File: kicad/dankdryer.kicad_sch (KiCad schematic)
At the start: 20 parts, among them J13 barreljack, J9 UART, SW2 boot, U1 AP63203WU, U6 ESP32-C6-MINI-1U

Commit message: tighten
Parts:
- L1: value 2.2u -> 3.9u
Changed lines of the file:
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@@
 			)
 		)
-		(property "Value" "2.2u"
+		(property "Value" "3.9u"
 			(at 109.22 39.37 90)
 			(effects

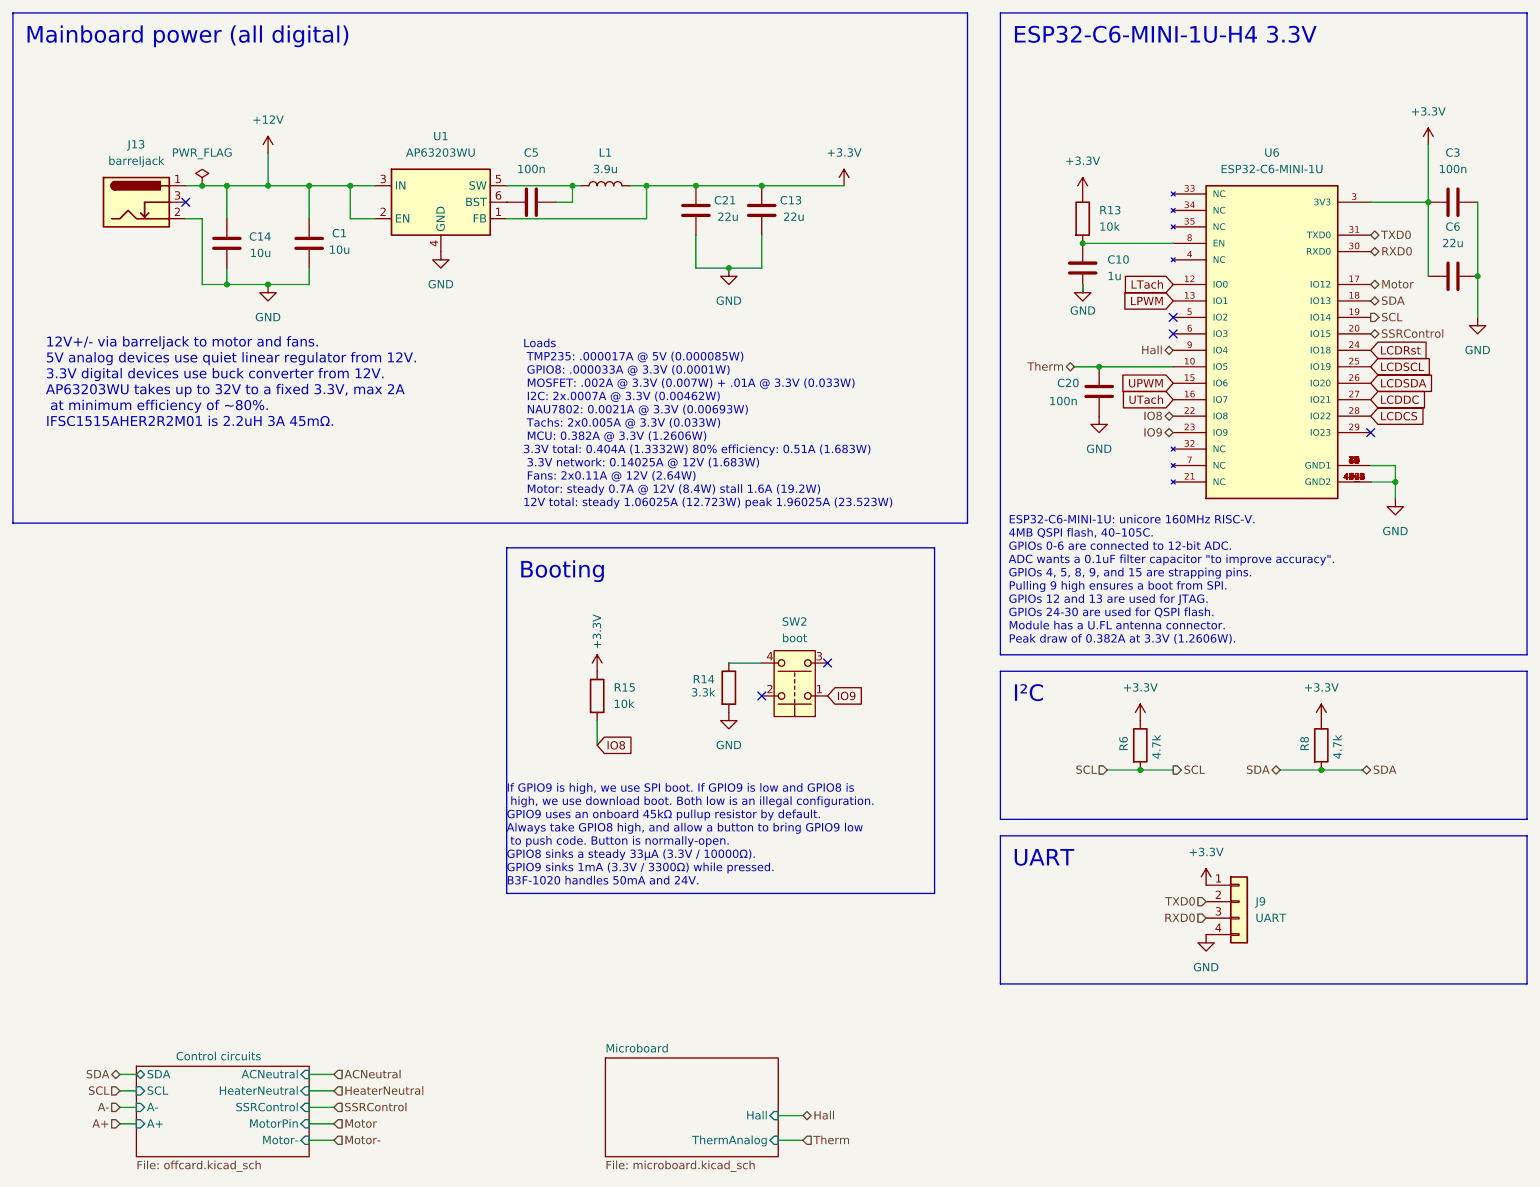
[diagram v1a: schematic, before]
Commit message: back to the tps62132rtgr after all. efficiency!
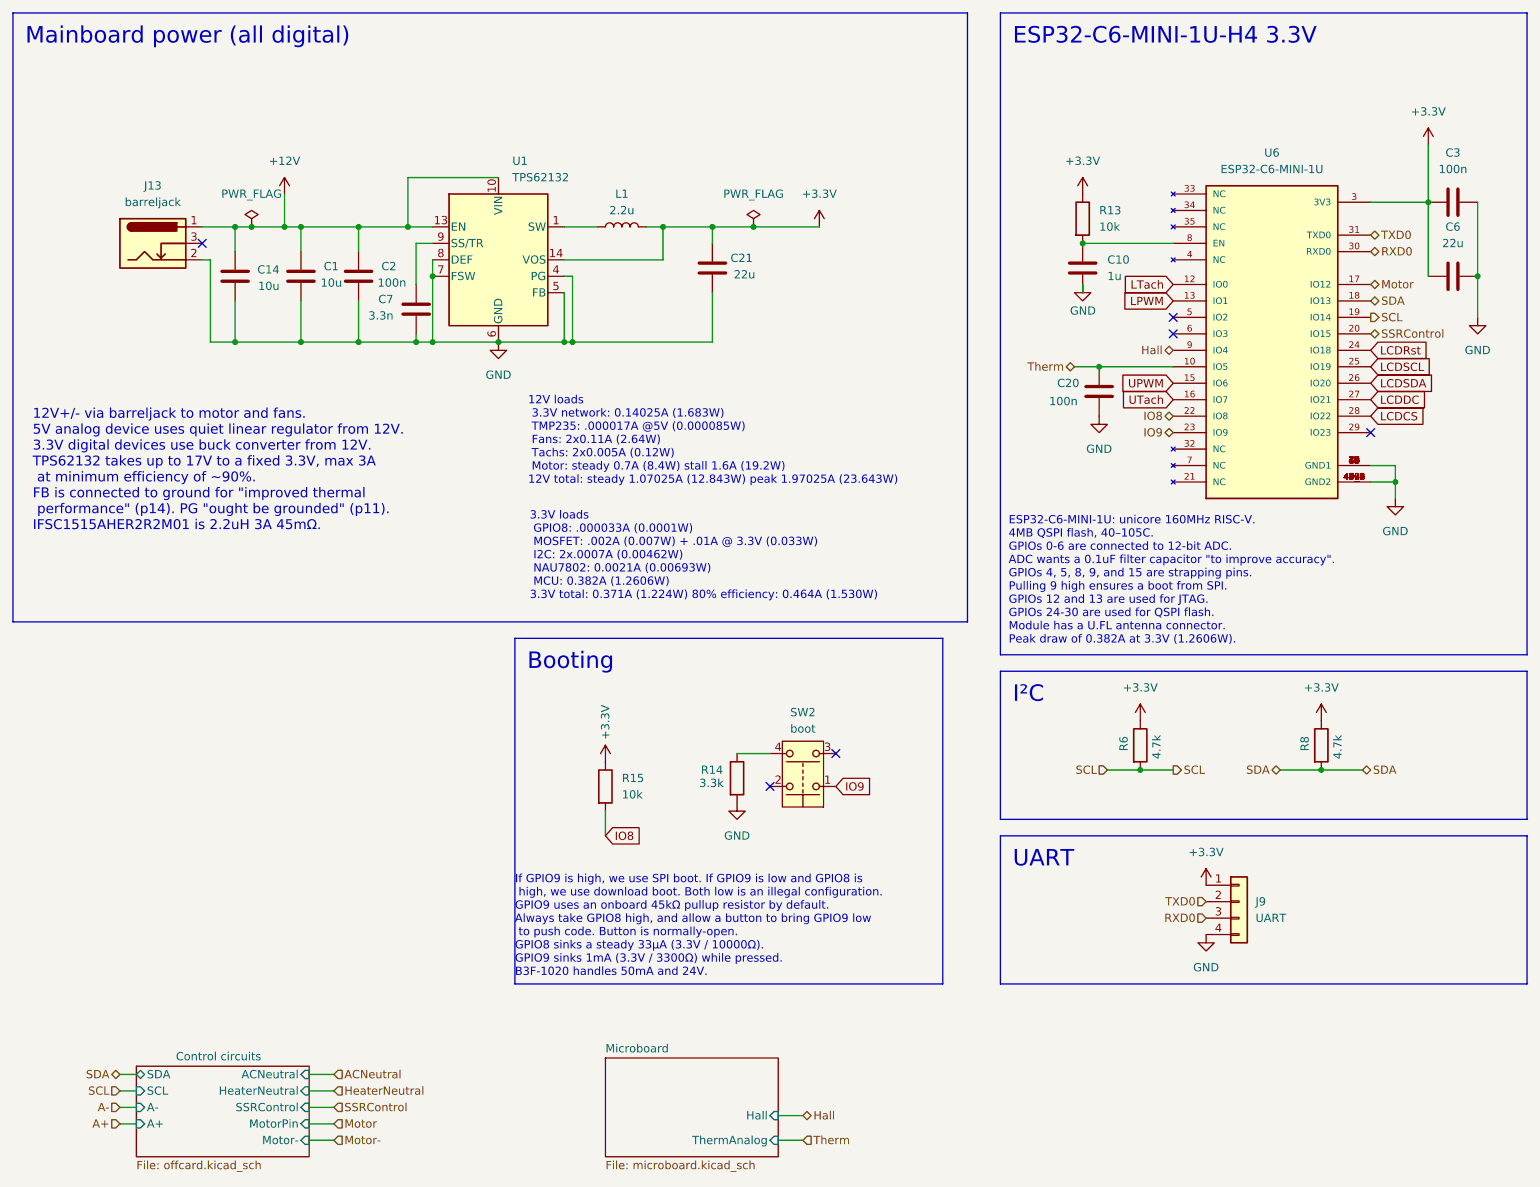
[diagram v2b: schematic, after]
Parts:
- removed C13: 22u, Capacitor_SMD:C_0805_2012Metric_Pad1.18x1.45mm_HandSolder, symbol Device:C
- removed C5: 100n, Capacitor_SMD:C_0805_2012Metric_Pad1.18x1.45mm_HandSolder, symbol Device:C
- removed U1: AP63203WU, Package_TO_SOT_SMD:TSOT-23-6, symbol Regulator_Switching:AP63203WU
- added C2: 100n, Capacitor_SMD:C_0805_2012Metric_Pad1.18x1.45mm_HandSolder, symbol Device:C
- added C7: 3.3n, Capacitor_SMD:C_0805_2012Metric_Pad1.18x1.45mm_HandSolder, symbol Device:C
- added U1: TPS62132, Package_DFN_QFN:VQFN-16-1EP_3x3mm_P0.5mm_EP1.68x1.68mm_ThermalVias, symbol Regulator_Switching:TPS62132
- L1: value 3.9u -> 2.2u
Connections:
- net +12V: now also C2.1, U1.10 (VIN), U1.11 (VIN), U1.12 (VIN), U1.13 (EN)
- net +3.3V: now also U1.14 (VOS)
- net GND: now also C2.2, C7.2, U1.15 (GND), U1.16 (GND), U1.17 (GND), U1.4 (PG), U1.5 (FB), U1.6 (GND), U1.7 (FSW), U1.8 (DEF)
- net at L1.1: now also U1.1 (SW), U1.2 (SW), U1.3 (SW)
- new net: C7.1, U1.9 (SS/TR)
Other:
- note added: "12V loads 3.3V network: 0.14025A (1.683W) TMP235: .000017A @5V (0.000085W) Fans: 2x0.11A (2.64W) Tachs: 2x0.005A (0.12W) Motor: steady 0.7A (8.4W) stall 1.6A (19.2W) 12V total: steady 1.07025A (12.843W) peak 1.97025A (23.643W)"
- note added: "12V+/- via barreljack to motor and fans. 5V analog device uses quiet linear regulator from 12V. 3.3V digital devices use buck converter from 12V. TPS62132 takes up to 17V to a fixed 3.3V, max 3A at minimum efficiency of ~90%. FB is connected to ground for "improved thermal performance" (p14). PG "ought be grounded" (p11). IFSC1515AHER2R2M01 is 2.2uH 3A 45mΩ."
- note added: "3.3V loads GPIO8: .000033A (0.0001W) MOSFET: .002A (0.007W) + .01A @ 3.3V (0.033W) I2C: 2x.0007A (0.00462W) NAU7802: 0.0021A (0.00693W) MCU: 0.382A (1.2606W) 3.3V total: 0.371A (1.224W) 80% efficiency: 0.464A (1.530W)"
- note removed: "12V+/- via barreljack to motor and fans. 5V analog devices use quiet linear regulator from 12V. 3.3V digital devices use buck converter from 12V. AP63203WU takes up to 32V to a fixed 3.3V, max 2A at minimum efficiency of ~80%. IFSC1515AHER2R2M01 is 2.2uH 3A 45mΩ."
- note removed: "Loads TMP235: .000017A @ 5V (0.000085W) GPIO8: .000033A @ 3.3V (0.0001W) MOSFET: .002A @ 3.3V (0.007W) + .01A @ 3.3V (0.033W) I2C: 2x.0007A @ 3.3V (0.00462W) NAU7802: 0.0021A @ 3.3V (0.00693W) Tachs: 2x0.005A @ 3.3V (0.033W) MCU: 0.382A @ 3.3V (1.2606W) 3.3V total: 0.404A (1.3332W) 80% efficiency: 0.51A (1.683W) 3.3V network: 0.14025A @ 12V (1.683W) Fans: 2x0.11A @ 12V (2.64W) Motor: steady 0.7A 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"
- moved on the sheet: C1, C14, C21, J13, L1, R14, R15, SW2

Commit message: [kicad] pcb v2.0.0 as sent to jlcpcb
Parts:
- L1: footprint dank:IND_IFSC_1515AH_VIS -> Inductor_SMD:L_Sunlord_SWPA4030S
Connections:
- net +3.3V: now also U1.7 (FSW)
- net GND: no longer U1.7 (FSW)
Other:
- sheet Control circuits ports: added none; removed Motor-
- note added: "12V+/- via barreljack to motor, fans, and thermometer. 3.3V digital devices use buck converter from 12V. TPS62132 takes up to 17V to a fixed 3.3V, max 3A at minimum efficiency of ~90%. FB is connected to ground for "improved thermal performance" (p14). PG "ought be grounded" (p11). IFSC1515AHER2R2M01 is 2.2uH 3.1A max 45mΩ DCR. FSW must be low at startup, but can then be brought high to reduce sw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"
- note removed: "12V+/- via barreljack to motor and fans. 5V analog device uses quiet linear regulator from 12V. 3.3V digital devices use buck converter from 12V. TPS62132 takes up to 17V to a fixed 3.3V, max 3A at minimum efficiency of ~90%. FB is connected to ground for "improved thermal performance" (p14). PG "ought be grounded" (p11). IFSC1515AHER2R2M01 is 2.2uH 3A 45mΩ."
- moved on the sheet: C1, C14, C2, C21, C7, J13

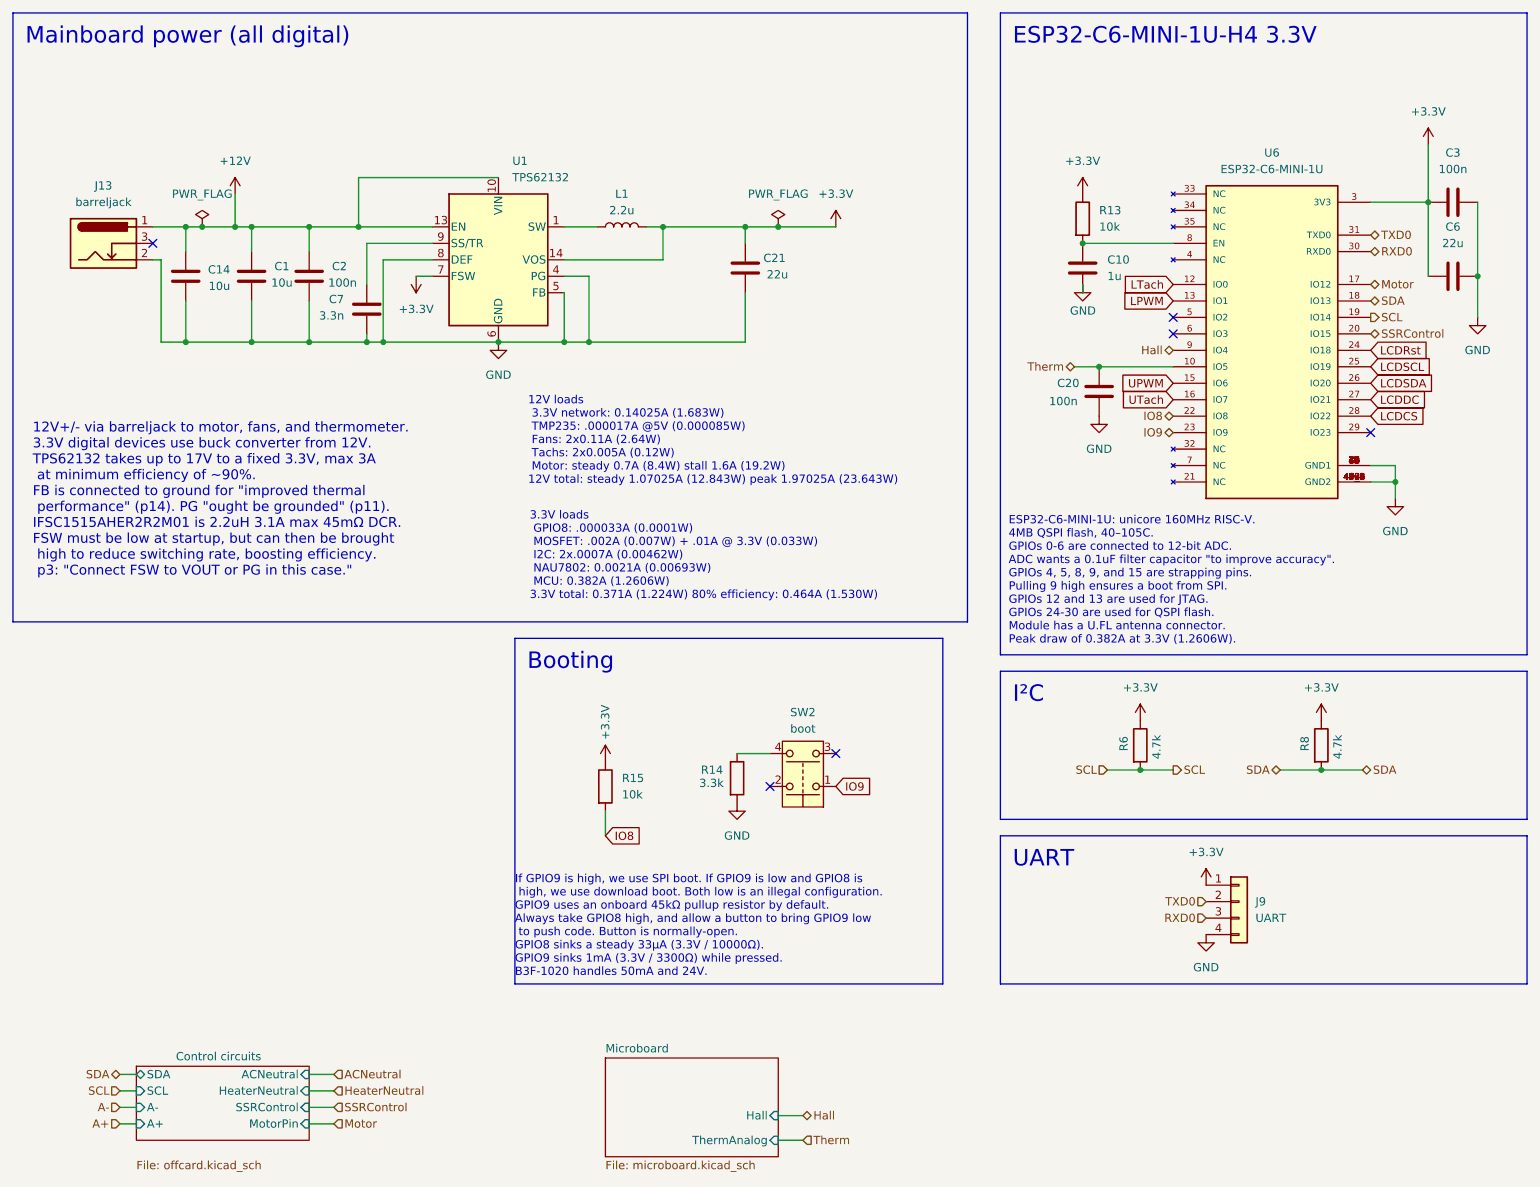
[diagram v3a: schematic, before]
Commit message: change 330 ohm resistors to 1206
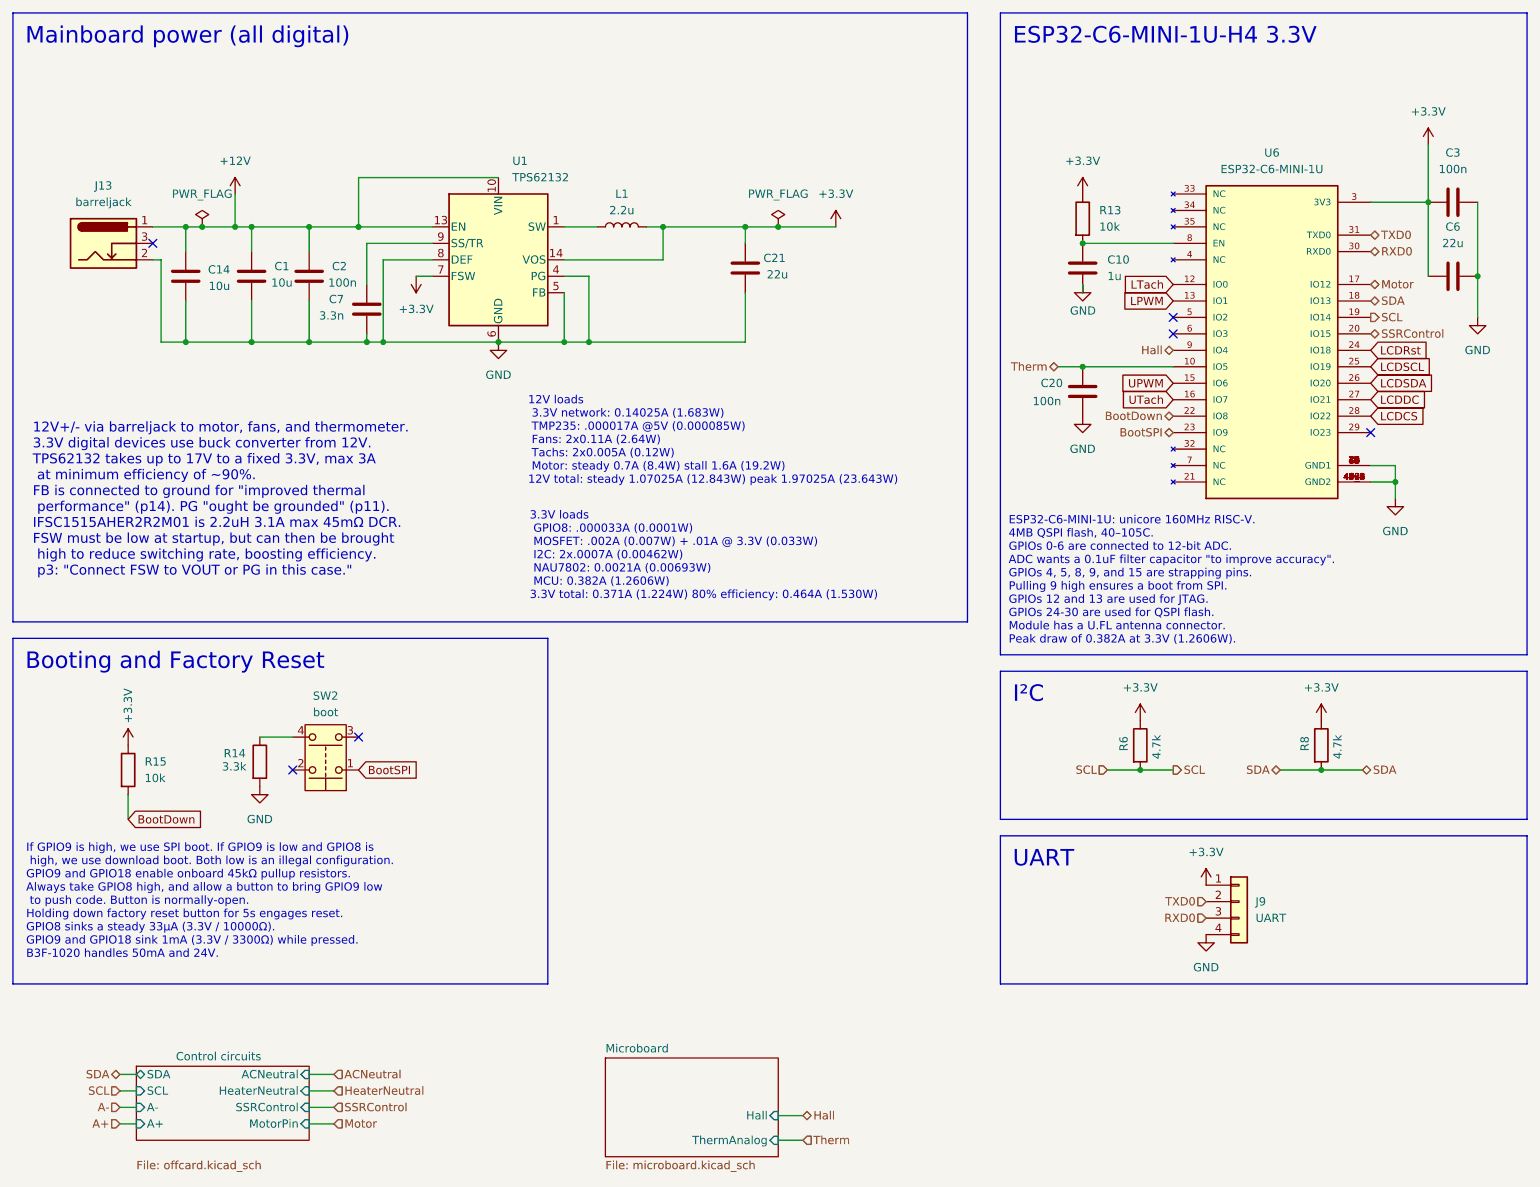
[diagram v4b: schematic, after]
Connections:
- net IO8 renamed BootDown
- net IO9 renamed BootSPI
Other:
- note added: "If GPIO9 is high, we use SPI boot. If GPIO9 is low and GPIO8 is high, we use download boot. Both low is an illegal configuration. GPIO9 and GPIO18 enable onboard 45kΩ pullup resistors. Always take GPIO8 high, and allow a button to bring GPIO9 low to push code. Button is normally-open. Holding down factory reset button for 5s engages reset. GPIO8 sinks a steady 33μA (3.3V / 10000Ω). GPIO9 and GPIO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"
- note removed: "If GPIO9 is high, we use SPI boot. If GPIO9 is low and GPIO8 is high, we use download boot. Both low is an illegal configuration. GPIO9 uses an onboard 45kΩ pullup resistor by default. Always take GPIO8 high, and allow a button to bring GPIO9 low to push code. Button is normally-open. GPIO8 sinks a steady 33μA (3.3V / 10000Ω). GPIO9 sinks 1mA (3.3V / 3300Ω) while pressed. B3F-1020 handles 50mA an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"
- moved on the sheet: C20, R14, R15, SW2

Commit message: put your boot down
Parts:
- removed U1: TPS62132, Package_DFN_QFN:VQFN-16-1EP_3x3mm_P0.5mm_EP1.68x1.68mm_ThermalVias, symbol Regulator_Switching:TPS62132
- added U4: TPS62132RGTR, Package_DFN_QFN:VQFN-16-1EP_3x3mm_P0.5mm_EP1.68x1.68mm_ThermalVias, symbol dank:TPS62132RGTR
- C1, C14, C2, C20, C7: footprint Capacitor_SMD:C_0805_2012Metric_Pad1.18x1.45mm_HandSolder -> Capacitor_SMD:C_1206_3216Metric_Pad1.33x1.80mm_HandSolder
- R13, R14, R15: footprint Resistor_SMD:R_0805_2012Metric_Pad1.20x1.40mm_HandSolder -> Resistor_SMD:R_1206_3216Metric_Pad1.30x1.75mm_HandSolder
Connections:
- net +12V: now also C2.2, U4.10 (AVIN), U4.11 (PVIN), U4.12 (PVIN__1), U4.13 (EN); no longer C2.1
- net +3.3V: now also U4.14 (VOS), U4.7 (FSW)
- net GND: now also C2.1, U4.15 (PGND), U4.16 (PGND__1), U4.17 (PGND__2), U4.4 (PG), U4.5 (FB), U4.6 (AGND), U4.8 (DEF); no longer C2.2
- net at C7.1: now also U4.9 (SS/TR)
- net at L1.1: now also U4.1 (SW), U4.2 (SW__1), U4.3 (SW__2)
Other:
- sheet Control circuits ports: added LPWM, LTach, UPWM, UTach; removed A+, A-
- moved on the sheet: C1, C10, C14, C2, C20, C21, C3, C6, C7, J13, J9, L1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
